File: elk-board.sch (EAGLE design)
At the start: 199 parts, among them IC1 KLM8G1GESD-B03P, IC10 MP2143DJ-LF-P, IC2 ALLWINNER--H3, IC3 SY6280, IC4 K4B4G1646D-BCK0, IC5 RT8059GJ5, IC6 RT8059GJ5, IC7 SY8089A, IC8 NCP803SN263T1G, IC9 RT8059GJ5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

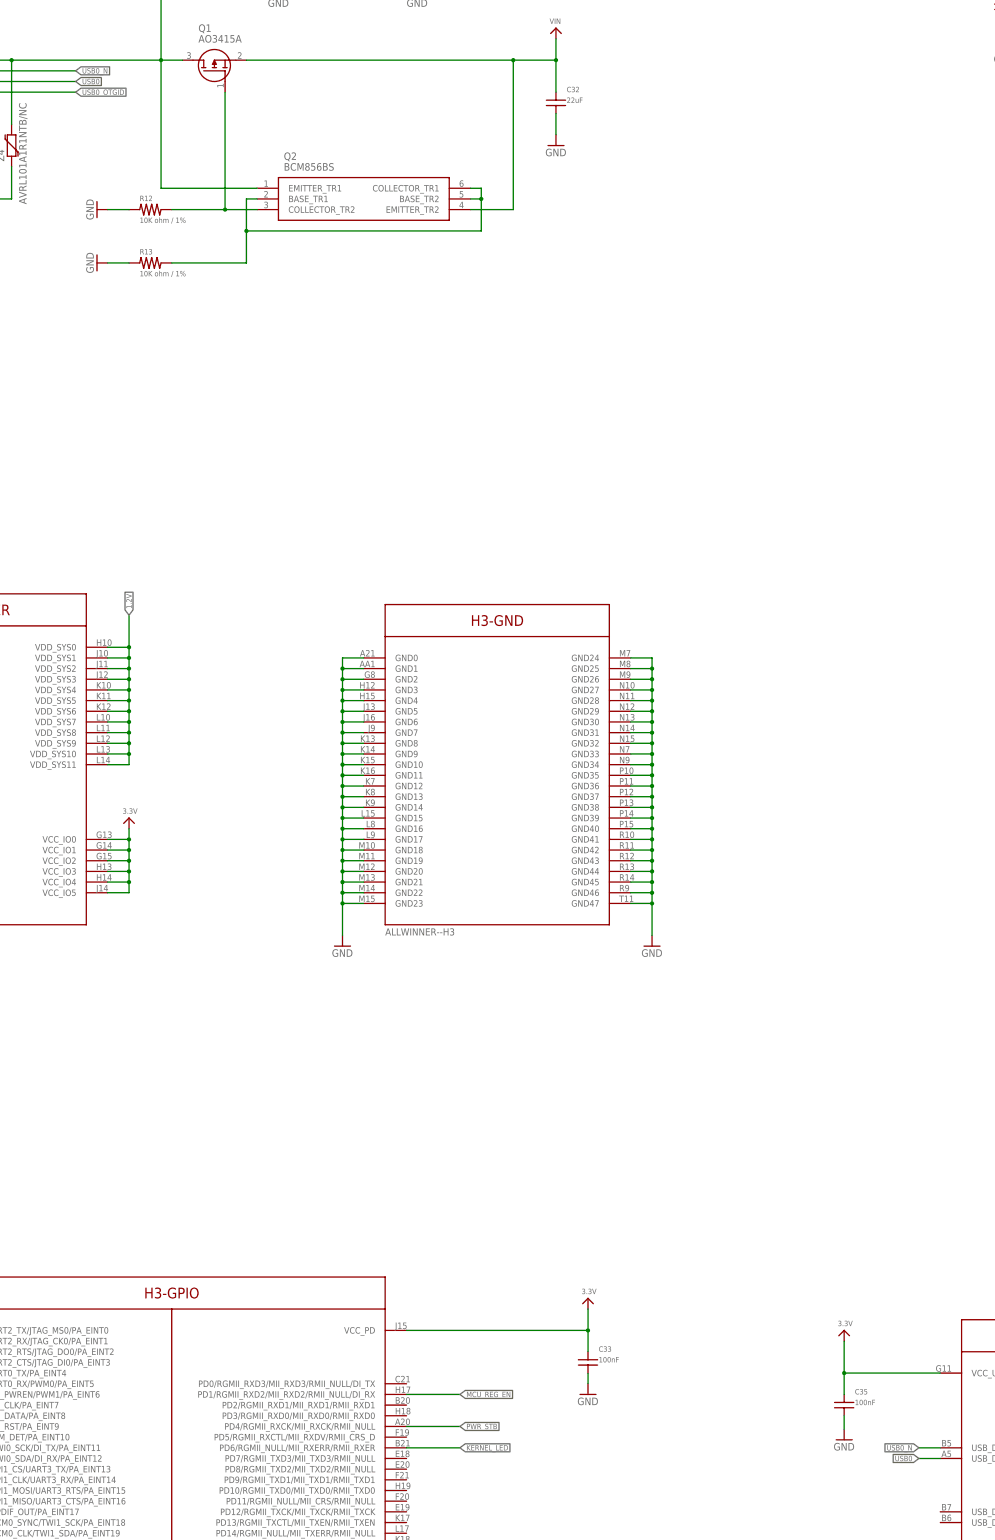
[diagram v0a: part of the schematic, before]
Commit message: 90ohm Impedence Control Enhancment
USB Differenctial Pair
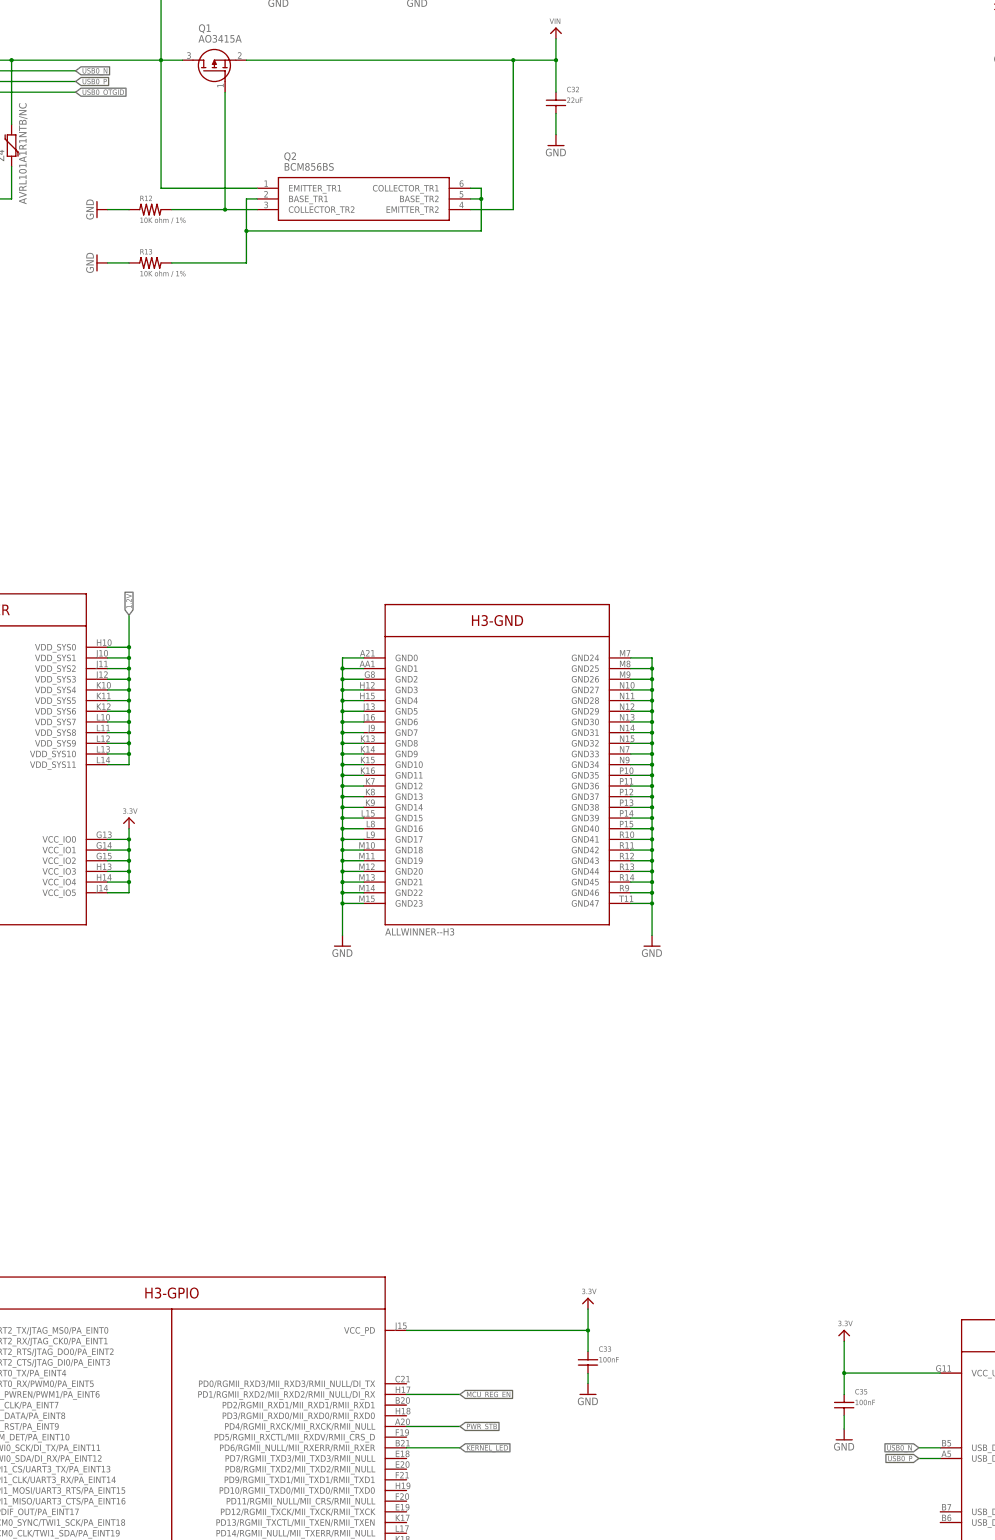
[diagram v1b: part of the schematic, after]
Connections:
- net USB0 renamed USB0_P
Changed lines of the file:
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@@
 </segment>
 </net>
-<net name="USB0" class="7">
+<net name="USB0_P" class="7">
 <segment>
 <pinref part="IC2" gate="G$7" pin="USB_DP0"/>
